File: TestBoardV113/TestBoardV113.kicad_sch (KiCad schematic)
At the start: 94 parts, among them J1 Conn_01x02_Socket, J10 Conn_01x02_Pin, J11 Conn_01x02_Pin, J12 Conn_01x02_Pin, J13 Conn_02x03_Odd_Even, J14 Conn_02x03_Odd_Even, J15 Conn_01x02_Pin, J16 Conn_02x03_Odd_Even, J17 Conn_01x01_Pin, J18 Conn_01x28_Socket, J19 Conn_01x01_Pin, J2 Conn_02x06_Odd_Even, J20 Conn_01x01_Pin, J21 Conn_01x02_Pin, J22 Conn_01x02_Socket, J23 Conn_01x28_Socket, J24 Conn_01x01_Pin, J25 Conn_01x02_Pin, J26 Conn_02x03_Odd_Even, J27 Conn_01x02_Pin, J28 Conn_01x02_Socket, J3 Conn_01x02_Pin, J4 Conn_01x02_Pin, J5 Conn_01x02_Pin, J6 Conn_01x02_Pin, J7 Conn_01x02_Pin, J8 Conn_01x02_Pin, J9 Conn_01x02_Pin, SW1 SW_DIP_x07, U3 NCP705MTADJTCG, U4 TAR5SxxU_SOT353F, U5 TXB0104PW, U6 TXB0104PW

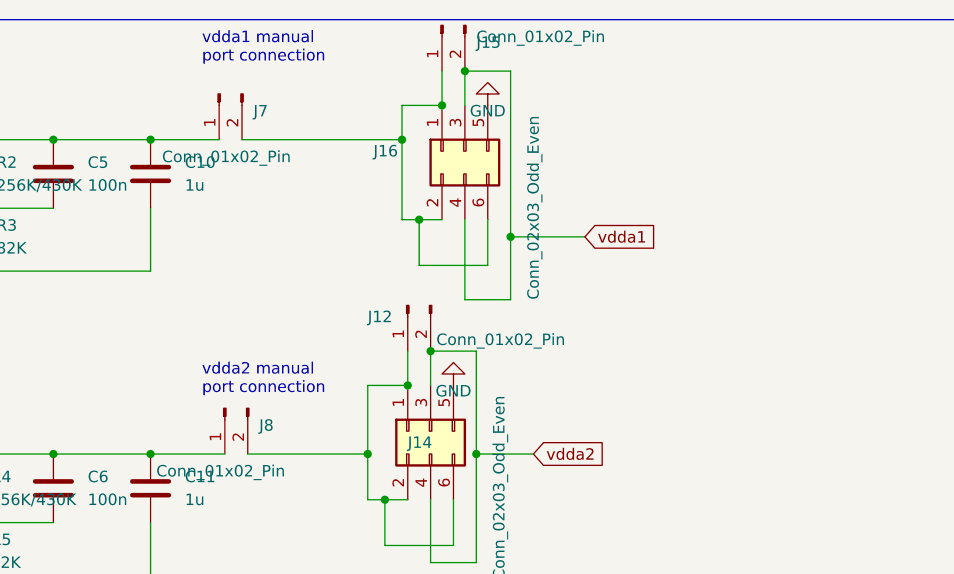
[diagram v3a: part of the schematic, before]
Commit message: Changes
Test Resistors from 0805 to 2010
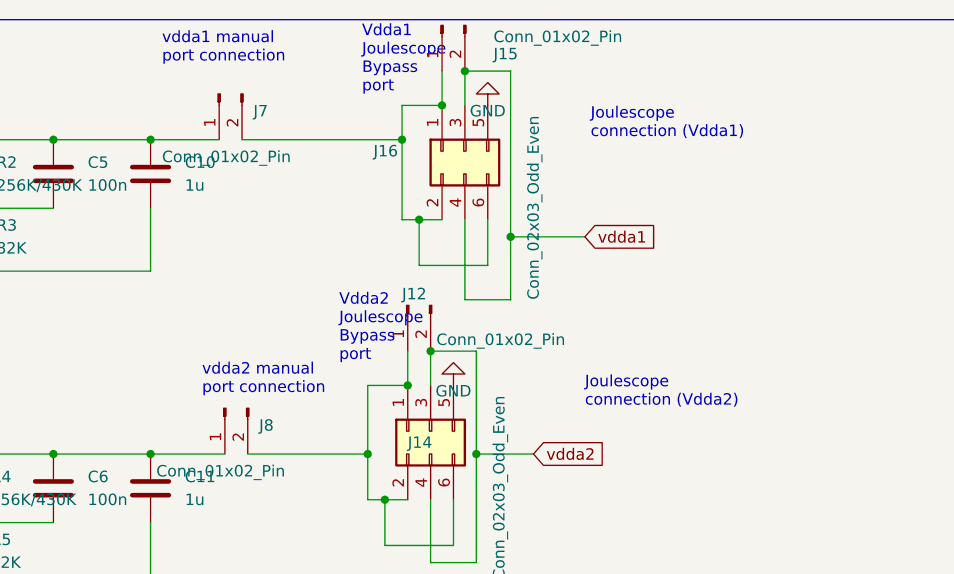
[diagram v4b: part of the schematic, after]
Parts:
- R10, R11, R12, R13, R14, R8, R9: footprint Resistor_SMD:R_1206_3216Metric -> Resistor_SMD:R_2010_5025Metric
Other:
- note added: "Joulescope connection (Vdda1)"
- note added: "Joulescope connection (Vdda2)"
- note added: "Vdda1 Joulescope Bypass port"
- note added: "Vdda2 Joulescope Bypass port"
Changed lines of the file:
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@@
     (effects (font (size 1.27 1.27)) (justify left bottom))
   )
+  (text "Vdda2 \nJoulescope \nBypass \nport\n" (at 140.97 53.34 0)
+    (effects (font (size 1.27 1.27)) (justify left bottom))
+  )
   (text "PWM D5-D8 3V3 input " (at 163.83 217.17 90)
     (effects (font (size 1.27 1.27)) (justify left bottom))
@@
     (effects (font (size 1.27 1.27)) (justify left bottom))
   )
+  (text "Joulescope \nconnection (Vdda1)\n" (at 168.91 28.575 0)
+    (effects (font (size 1.27 1.27)) (justify left bottom))
+  )
   (text "VH Joulescope Bypass \nport\n" (at 139.7 82.55 0)
     (effects (font (size 1.27 1.27)) (justify left bottom))
@@
     (effects (font (size 1.27 1.27)) (justify left bottom))
   )
+  (text "Vdda1 \nJoulescope \nBypass \nport\n" (at 143.51 23.495 0)
+    (effects (font (size 1.27 1.27)) (justify left bottom))
+  )
   (text "PWM Translation\n" (at 24.765 233.68 0)
     (effects (font (size 3.81 3.81)) (justify left bottom))
@@
     (effects (font (size 1.27 1.27)) (justify left bottom))
   )
+  (text "Joulescope \nconnection (Vdda2)\n" (at 168.275 58.42 0)
+    (effects (font (size 1.27 1.27)) (justify left bottom))
+  )
   (text "1.8 Lvl shifters manual\nport connection\n" (at 128.905 129.54 0)
     (effects (font (size 1.27 1.27)) (justify left bottom))
@@
     (effects (font (size 1.27 1.27)) (justify left bottom))
   )
-  (text "vdda1 manual\nport connection\n\n" (at 125.73 22.225 0)
+  (text "vdda1 manual\nport connection\n\n" (at 121.285 22.225 0)
     (effects (font (size 1.27 1.27)) (justify left bottom))
   )
@@
       (effects (font (size 1.27 1.27)) (justify left))
     )
-    (property "Footprint" "Resistor_SMD:R_1206_3216Metric" (at 361.442 81.915 90)
+    (property "Footprint" "Resistor_SMD:R_2010_5025Metric" (at 361.442 81.915 90)
       (effects (font (size 1.27 1.27)) hide)
     )
@@
       (effects (font (size 1.27 1.27)) (justify left))
     )
-    (property "Footprint" "Resistor_SMD:R_1206_3216Metric" (at 368.427 81.915 90)
+    (property "Footprint" "Resistor_SMD:R_2010_5025Metric" (at 368.427 81.915 90)
       (effects (font (size 1.27 1.27)) hide)
     )
@@
       (effects (font (size 1.27 1.27)) (justify left))
     )
-    (property "Footprint" "Resistor_SMD:R_1206_3216Metric" (at 355.092 81.915 90)
+    (property "Footprint" "Resistor_SMD:R_2010_5025Metric" (at 355.092 81.915 90)
       (effects (font (size 1.27 1.27)) hide)
     )
@@
       (effects (font (size 1.27 1.27)) (justify left))
     )
-    (property "Footprint" "Resistor_SMD:R_1206_3216Metric" (at 351.917 81.915 90)
+    (property "Footprint" "Resistor_SMD:R_2010_5025Metric" (at 351.917 81.915 90)
       (effects (font (size 1.27 1.27)) hide)
     )
@@
       (effects (font (size 1.27 1.27)) (justify left))
     )
-    (property "Footprint" "Resistor_SMD:R_1206_3216Metric" (at 371.602 81.915 90)
+    (property "Footprint" "Resistor_SMD:R_2010_5025Metric" (at 371.602 81.915 90)
       (effects (font (size 1.27 1.27)) hide)
     )
@@
   (symbol (lib_id "Connector:Conn_01x02_Pin") (at 152.4 15.875 90) (mirror x) (unit 1)
     (in_bom yes) (on_board yes) (dnp no)
-    (property "Reference" "J15" (at 156.21 17.78 90)
+    (property "Reference" "J15" (at 158.115 19.05 90)
       (effects (font (size 1.27 1.27)) (justify right))
     )
-    (property "Value" "Conn_01x02_Pin" (at 156.21 17.145 90)
+    (property "Value" "Conn_01x02_Pin" (at 158.115 17.145 90)
       (effects (font (size 1.27 1.27)) (justify right))
     )
@@
   (symbol (lib_id "Connector:Conn_01x02_Pin") (at 148.59 46.99 90) (mirror x) (unit 1)
     (in_bom yes) (on_board yes) (dnp no)
-    (property "Reference" "J12" (at 144.145 48.26 90)
+    (property "Reference" "J12" (at 147.955 45.72 90)
       (effects (font (size 1.27 1.27)) (justify right))
     )
@@
       (effects (font (size 1.27 1.27)) (justify left))
     )
-    (property "Footprint" "Resistor_SMD:R_1206_3216Metric" (at 365.252 81.915 90)
+    (property "Footprint" "Resistor_SMD:R_2010_5025Metric" (at 365.252 81.915 90)
       (effects (font (size 1.27 1.27)) hide)
     )
@@
       (effects (font (size 1.27 1.27)) (justify left))
     )
-    (property "Footprint" "Resistor_SMD:R_1206_3216Metric" (at 358.267 81.915 90)
+    (property "Footprint" "Resistor_SMD:R_2010_5025Metric" (at 358.267 81.915 90)
       (effects (font (size 1.27 1.27)) hide)
     )

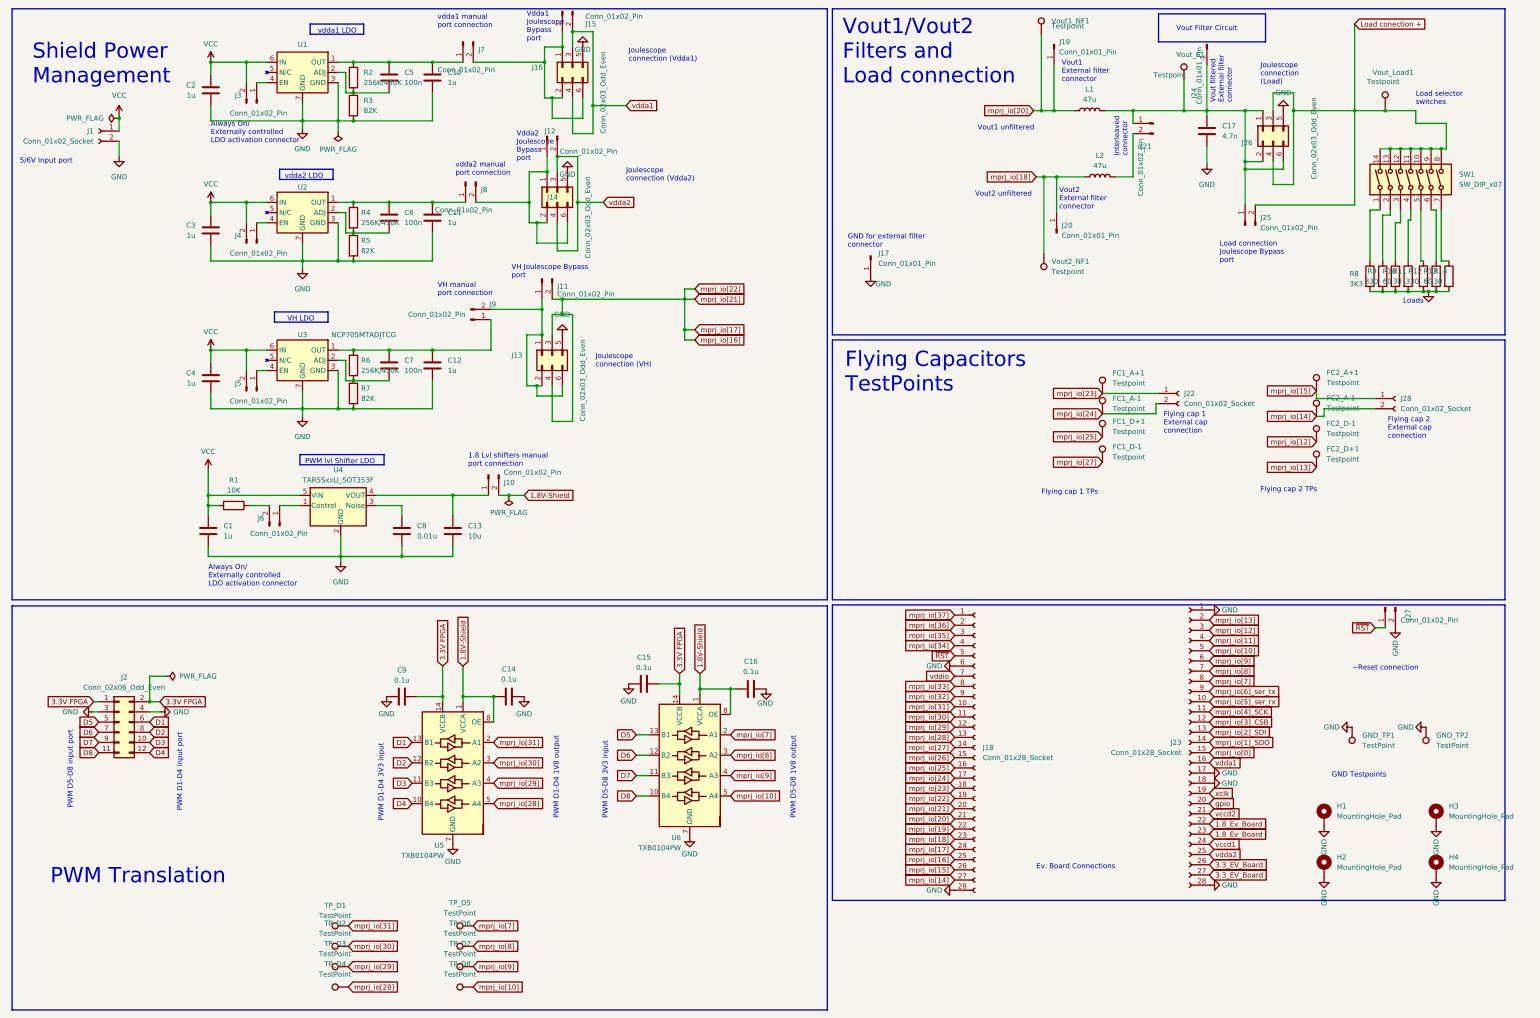
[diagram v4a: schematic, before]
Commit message: Changes
added real resistances values for the dip switch resistances and made the schematic more clear to read. Changed the fpga connector footprint for D1-D8 to avoid warnings
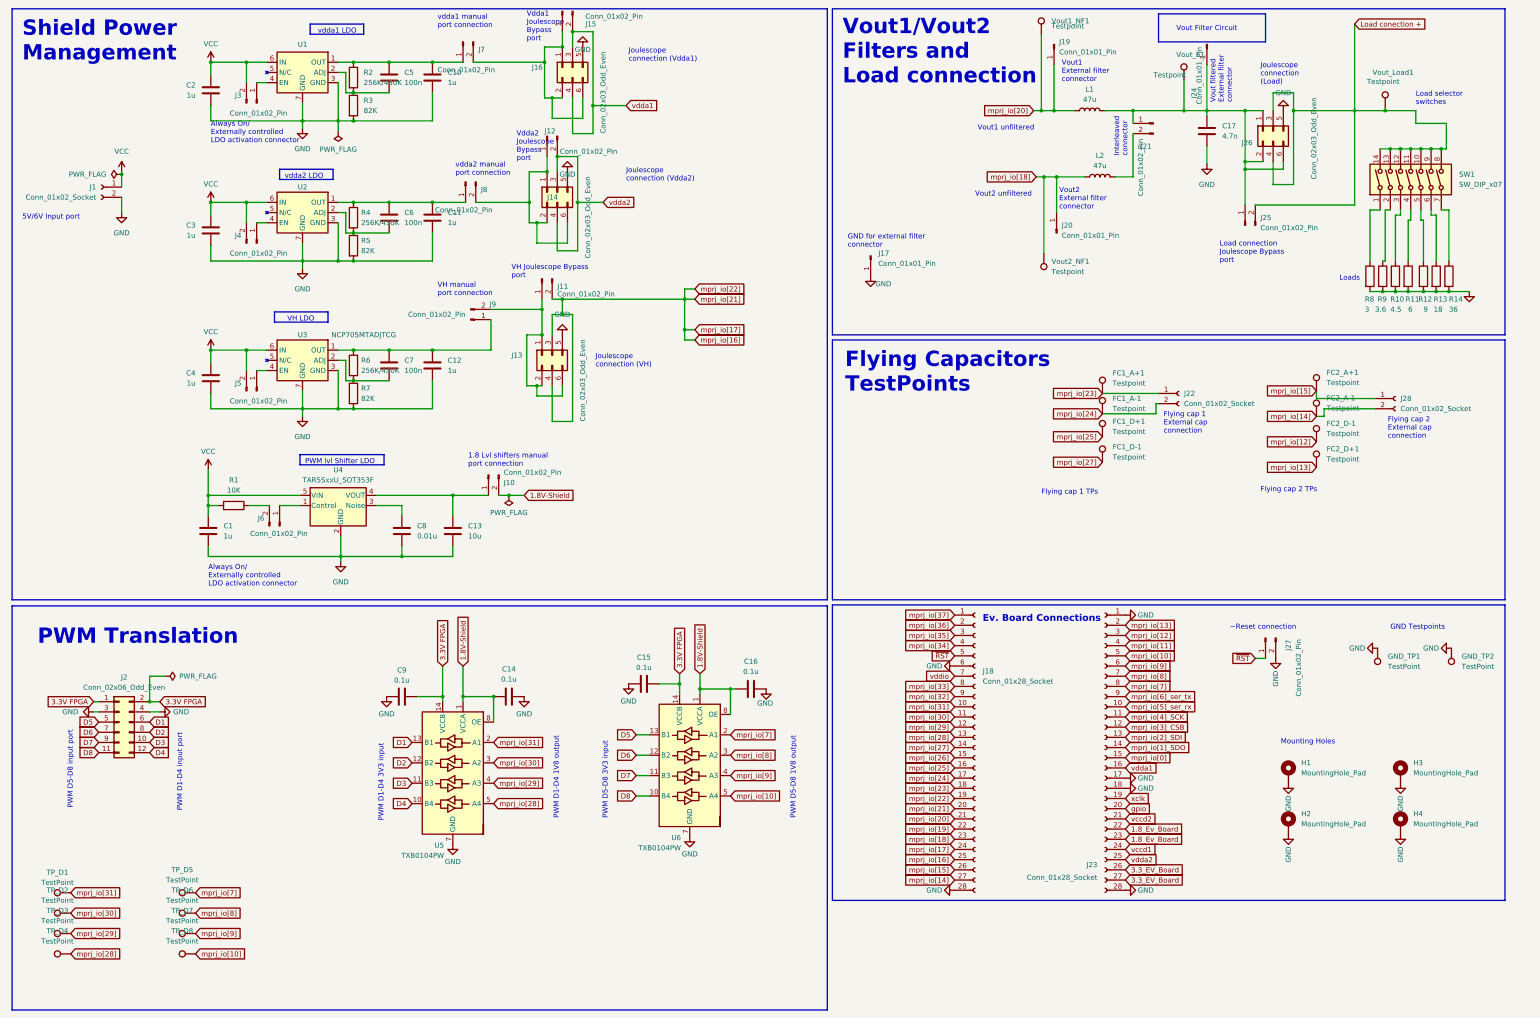
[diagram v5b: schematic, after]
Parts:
- J2: footprint Connector_PinHeader_2.54mm:PinHeader_2x06_P2.54mm_Horizontal -> Connector_PinHeader_2.54mm:PinHeader_2x06_P2.54mm_Vertical
- R10: value 60 -> 4.5
- R11: value 30 -> 6
- R12: value 330 -> 9
- R13: value 60 -> 18
- R14: value 30 -> 36
- R8: value 3K3 -> 3
- R9: value 330 -> 3.6
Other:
- note added: "5V/6V Input port"
- note added: "Mounting Holes"
- note removed: "5/6V Input port"
- moved on the sheet: GND_TP1, GND_TP2, H1, H2, H3, H4, J1, J23, J27, TP_D1, TP_D2, TP_D3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

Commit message: Changes
increased tracks width, change some component placements for better dynamic response, added a connection to ground for vdda1, vdda2 and VH
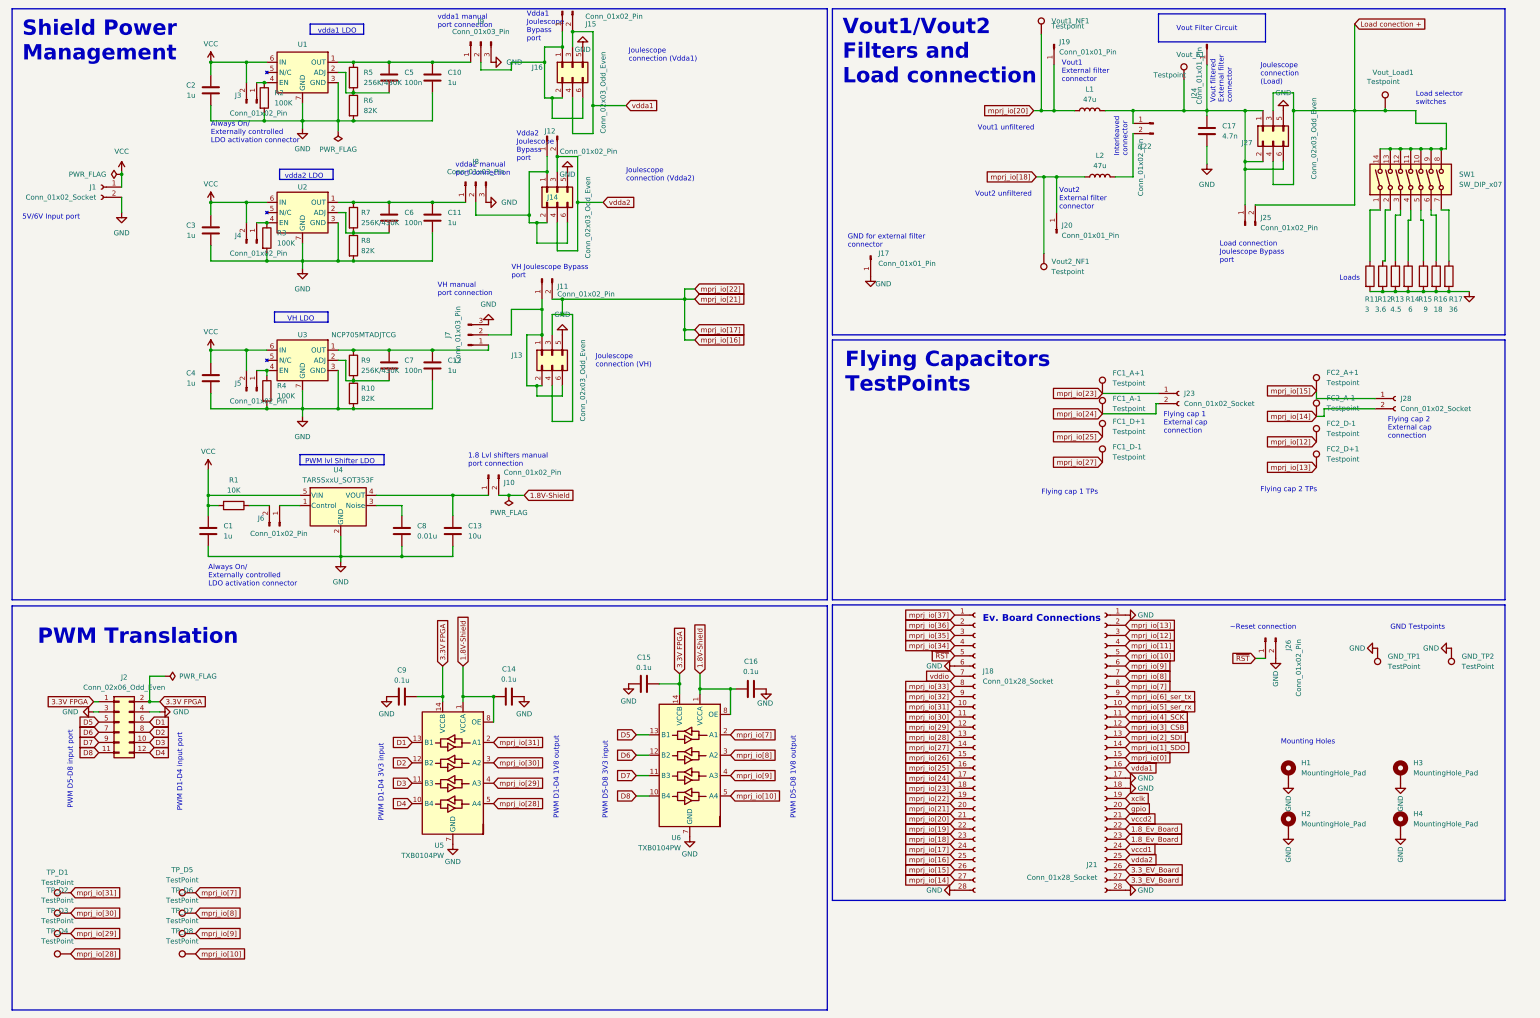
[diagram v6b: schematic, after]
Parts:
- removed J7, J8, J9: Conn_01x02_Pin, Connector_PinHeader_2.54mm:PinHeader_1x02_P2.54mm_Vertical, symbol Connector:Conn_01x02_Pin
- added J7, J8, J9: Conn_01x03_Pin, Connector_PinHeader_2.54mm:PinHeader_1x03_P2.54mm_Vertical, symbol Connector:Conn_01x03_Pin
- added R2, R3, R4: 100K, Resistor_SMD:R_0805_2012Metric, symbol Device:R
- renumbered J23 to J21, J21 to J22, J22 to J23, J27 to J26, J26 to J27, R7 to R10, R8 to R11, R9 to R12, R10 to R13, R11 to R14, R12 to R15, R13 to R16, R14 to R17, R2 to R5, R3 to R6, R4 to R7, R5 to R8, R6 to R9
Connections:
- net GND: now also J7.3 (Pin_3), J8.3 (Pin_3), J9.3 (Pin_3), R2.2, R3.2, R4.2
- net at C10.1, C5.1, R5.1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: now also J9.1 (Pin_1)
- net at C11.1, C6.1, R7.1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: now also J8.1 (Pin_1)
- net at J12.1 (Pin_1), J14.1 (Pin_1), J14.2 (Pin_2)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: now also J8.2 (Pin_2)
- net at C12.1, C7.1, R9.1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: now also J7.1 (Pin_1)
- net at J11.1 (Pin_1), J13.1 (Pin_1), J13.2 (Pin_2)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: now also J7.2 (Pin_2)
- net at J4.1 (Pin_1), U2.4 (EN): now also R3.1
- net at J15.1 (Pin_1), J16.1 (Pin_1), J16.2 (Pin_2)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: now also J9.2 (Pin_2)
- net at J3.1 (Pin_1), U1.4 (EN): now also R2.1
- net at J5.1 (Pin_1), U3.4 (EN): now also R4.1
